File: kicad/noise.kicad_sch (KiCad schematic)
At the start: 9 parts, among them Q10 2N3904, Q9 2N3904

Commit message: component positioning mostly done
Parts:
- C51: footprint rumblesan-standard-parts:C_Rect_L7.0mm_W3.5mm_P5.00mm -> rumblesan-standard-parts:C_Rect_L7.0mm_W2.5mm_P5.00mm
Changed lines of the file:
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@@
     (property "Reference" "C51" (id 0) (at 93.98 72.8812 90))
     (property "Value" "100nF" (id 1) (at 93.98 75.4181 90))
-    (property "Footprint" "rumblesan-standard-parts:C_Rect_L7.0mm_W3.5mm_P5.00mm" (id 2) (at 92.71 73.025 90)
+    (property "Footprint" "rumblesan-standard-parts:C_Rect_L7.0mm_W2.5mm_P5.00mm" (id 2) (at 92.71 73.025 90)
       (effects (font (size 1.27 1.27)) hide)
     )

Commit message: initial layout done
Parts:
- C52: footprint rumblesan-standard-parts:C_Rect_L7.0mm_W3.5mm_P5.00mm -> rumblesan-standard-parts:C_Rect_L7.0mm_W2.5mm_P5.00mm
- Q10: value 2N3904 -> BC549C
- R120: value 1k -> 47r
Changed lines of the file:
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@@
       (effects (font (size 1.27 1.27)) (justify left))
     )
-    (property "Value" "2N3904" (id 1) (at 115.3414 80.4422 0)
+    (property "Value" "BC549C" (id 1) (at 115.3414 80.4422 0)
       (effects (font (size 1.27 1.27)) (justify left))
     )
@@
       (effects (font (size 1.27 1.27)) (justify left))
     )
-    (property "Value" "1k" (id 1) (at 114.808 91.8722 0)
+    (property "Value" "47r" (id 1) (at 114.808 91.8722 0)
       (effects (font (size 1.27 1.27)) (justify left))
     )
@@
     (property "Reference" "C52" (id 0) (at 123.19 66.5312 90))
     (property "Value" "47nF" (id 1) (at 123.19 69.0681 90))
-    (property "Footprint" "rumblesan-standard-parts:C_Rect_L7.0mm_W3.5mm_P5.00mm" (id 2) (at 121.92 66.675 90)
+    (property "Footprint" "rumblesan-standard-parts:C_Rect_L7.0mm_W2.5mm_P5.00mm" (id 2) (at 121.92 66.675 90)
       (effects (font (size 1.27 1.27)) hide)
     )

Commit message: Full rejig to use attiny for divider
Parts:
- removed Q9: 2N3904, rumblesan-standard-parts:TO-92_Inline_Wide, symbol Transistor_BJT:2N3904
- removed R116: 100k, rumblesan-standard-parts:R_Axial_DIN0207_L6.3mm_D2.5mm_P10.16mm_Horizontal, symbol rumblesan-standard-parts:R
- added Q9: BC547, rumblesan-standard-parts:TO-92_Inline_Wide, symbol Transistor_BJT:BC547
- added RV23: 200k, rumblesan-standard-parts:Potentiometer_THT_Bourns_3306P_Vertical, symbol rumblesan-standard-parts:R_Potentiometer_Trim
- C51: Spec ceramic C0G -> ceramic X7R
- C52: value 47nF -> 100nF; Spec ceramic C0G -> ceramic X7R
- R120: value 47r -> 22r
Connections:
- net GND: now also Q9.2 (B)
- net VCC: now also RV23.2
- net at C51.1: now also Q9.3 (E), RV23.1
- no-connect marks 1 -> 2
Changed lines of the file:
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@@
   )
   (no_connect (at 82.55 91.44))
+  (no_connect (at 82.55 64.77))
   (wire (pts (xy 113.03 60.96) (xy 113.03 63.5))
     (stroke (width 0) (type default) (color 0 0 0 0))
   )
-  (wire (pts (xy 82.55 76.2) (xy 82.55 78.74))
+  (wire (pts (xy 82.55 72.39) (xy 82.55 78.74))
     (stroke (width 0) (type default) (color 0 0 0 0))
   )
@@
     (stroke (width 0) (type default) (color 0 0 0 0))
   )
+  (wire (pts (xy 74.93 68.58) (xy 78.74 68.58))
+    (stroke (width 0) (type default) (color 0 0 0 0))
+  )
   (wire (pts (xy 127 72.39) (xy 132.08 72.39))
     (stroke (width 0) (type default) (color 0 0 0 0))
@@
     (stroke (width 0) (type default) (color 0 0 0 0))
   )
-  (wire (pts (xy 82.55 66.04) (xy 82.55 68.58))
-    (stroke (width 0) (type default) (color 0 0 0 0))
-  )
   (wire (pts (xy 113.03 72.39) (xy 113.03 73.66))
     (stroke (width 0) (type default) (color 0 0 0 0))
@@
   )
   (wire (pts (xy 71.12 86.36) (xy 71.12 92.71))
+    (stroke (width 0) (type default) (color 0 0 0 0))
+  )
+  (wire (pts (xy 74.93 59.69) (xy 74.93 68.58))
     (stroke (width 0) (type default) (color 0 0 0 0))
   )
@@
     )
     (pin "1")
+  )
+  (symbol (lib_id "rumblesan-standard-parts:R_Potentiometer_Trim") (at 82.55 68.58 180) (unit 1)
+    (in_bom yes) (on_board yes) (fields_autoplaced)
+    (property "Reference" "RV23" (id 0) (at 84.328 67.7453 0)
+      (effects (font (size 1.27 1.27)) (justify right))
+    )
+    (property "Value" "200k" (id 1) (at 84.328 70.2822 0)
+      (effects (font (size 1.27 1.27)) (justify right))
+    )
+    (property "Footprint" "rumblesan-standard-parts:Potentiometer_THT_Bourns_3306P_Vertical" (id 2) (at 82.55 68.58 0)
+      (effects (font (size 1.27 1.27)) hide)
+    )
+    (property "Datasheet" "~" (id 3) (at 82.55 68.58 0)
+      (effects (font (size 1.27 1.27)) hide)
+    )
+    (property "Name" "" (id 4) (at 78.74 78.74 0))
+    (property "Spec" "single turn" (id 5) (at 82.55 68.58 0)
+      (effects (font (size 1.27 1.27)) hide)
+    )
+    (pin "1")
+    (pin "2")
+    (pin "3")
   )
   (symbol (lib_id "rumblesan-standard-parts:R") (at 101.6 86.36 0) (unit 1)
@@
       (effects (font (size 1.27 1.27)) hide)
     )
-    (property "Spec" "ceramic C0G" (id 4) (at 93.98 74.93 90)
+    (property "Spec" "ceramic X7R" (id 4) (at 93.98 74.93 90)
       (effects (font (size 1.27 1.27)) hide)
     )
@@
     (pin "1")
   )
-  (symbol (lib_id "power:VCC") (at 82.55 66.04 0) (unit 1)
-    (in_bom yes) (on_board yes) (fields_autoplaced)
-    (property "Reference" "#PWR0162" (id 0) (at 82.55 69.85 0)
-      (effects (font (size 1.27 1.27)) hide)
-    )
-    (property "Value" "VCC" (id 1) (at 82.55 62.4642 0))
-    (property "Footprint" "" (id 2) (at 82.55 66.04 0)
-      (effects (font (size 1.27 1.27)) hide)
-    )
-    (property "Datasheet" "" (id 3) (at 82.55 66.04 0)
+  (symbol (lib_id "power:VCC") (at 74.93 59.69 0) (unit 1)
+    (in_bom yes) (on_board yes) (fields_autoplaced)
+    (property "Reference" "#PWR0162" (id 0) (at 74.93 63.5 0)
+      (effects (font (size 1.27 1.27)) hide)
+    )
+    (property "Value" "VCC" (id 1) (at 74.93 56.1142 0))
+    (property "Footprint" "" (id 2) (at 74.93 59.69 0)
+      (effects (font (size 1.27 1.27)) hide)
+    )
+    (property "Datasheet" "" (id 3) (at 74.93 59.69 0)
       (effects (font (size 1.27 1.27)) hide)
     )
@@
       (effects (font (size 1.27 1.27)) (justify left))
     )
-    (property "Value" "47r" (id 1) (at 114.808 91.8722 0)
+    (property "Value" "22r" (id 1) (at 114.808 91.8722 0)
       (effects (font (size 1.27 1.27)) (justify left))
     )
@@
     (pin "1")
   )
-  (symbol (lib_id "rumblesan-standard-parts:R") (at 82.55 72.39 0) (unit 1)
-    (in_bom yes) (on_board yes) (fields_autoplaced)
-    (property "Reference" "R116" (id 0) (at 84.328 71.5553 0)
-      (effects (font (size 1.27 1.27)) (justify left))
-    )
-    (property "Value" "100k" (id 1) (at 84.328 74.0922 0)
-      (effects (font (size 1.27 1.27)) (justify left))
-    )
-    (property "Footprint" "rumblesan-standard-parts:R_Axial_DIN0207_L6.3mm_D2.5mm_P10.16mm_Horizontal" (id 2) (at 85.09 74.93 90)
-      (effects (font (size 1.27 1.27)) hide)
-    )
-    (property "Datasheet" "~" (id 3) (at 88.9 72.39 90)
-      (effects (font (size 1.27 1.27)) hide)
-    )
-    (property "Tolerance" "1%" (id 4) (at 87.63 78.74 90)
-      (effects (font (size 1.27 1.27)) hide)
-    )
-    (property "Power" "0.5W" (id 5) (at 87.63 64.77 90)
-      (effects (font (size 1.27 1.27)) hide)
-    )
-    (property "Spec" "metal film" (id 6) (at 87.63 72.39 90)
-      (effects (font (size 1.27 1.27)) hide)
-    )
-    (pin "1")
-    (pin "2")
+  (symbol (lib_id "Transistor_BJT:BC547") (at 80.01 86.36 0) (mirror x) (unit 1)
+    (in_bom yes) (on_board yes) (fields_autoplaced)
+    (property "Reference" "Q9" (id 0) (at 84.8614 85.5253 0)
+      (effects (font (size 1.27 1.27)) (justify left))
+    )
+    (property "Value" "BC547" (id 1) (at 84.8614 88.0622 0)
+      (effects (font (size 1.27 1.27)) (justify left))
+    )
+    (property "Footprint" "rumblesan-standard-parts:TO-92_Inline_Wide" (id 2) (at 85.09 84.455 0)
+      (effects (font (size 1.27 1.27) italic) (justify left) hide)
+    )
+    (property "Datasheet" "https://www.onsemi.com/pub/Collateral/BC550-D.pdf" (id 3) (at 80.01 86.36 0)
+      (effects (font (size 1.27 1.27)) (justify left) hide)
+    )
+    (pin "1")
+    (pin "2")
+    (pin "3")
   )
   (symbol (lib_id "power:GND") (at 113.03 96.52 0) (mirror y) (unit 1)
@@
     (in_bom yes) (on_board yes) (fields_autoplaced)
     (property "Reference" "C52" (id 0) (at 123.19 66.5312 90))
-    (property "Value" "47nF" (id 1) (at 123.19 69.0681 90))
+    (property "Value" "100nF" (id 1) (at 123.19 69.0681 90))
     (property "Footprint" "rumblesan-standard-parts:C_Rect_L7.0mm_W2.5mm_P5.00mm" (id 2) (at 121.92 66.675 90)
       (effects (font (size 1.27 1.27)) hide)
@@
       (effects (font (size 1.27 1.27)) hide)
     )
-    (property "Spec" "ceramic C0G" (id 4) (at 123.19 68.58 90)
+    (property "Spec" "ceramic X7R" (id 4) (at 123.19 68.58 90)
       (effects (font (size 1.27 1.27)) hide)
     )
@@
     (pin "2")
   )
-  (symbol (lib_id "Transistor_BJT:2N3904") (at 80.01 86.36 0) (mirror x) (unit 1)
-    (in_bom yes) (on_board yes)
-    (property "Reference" "Q9" (id 0) (at 73.66 83.82 0)
-      (effects (font (size 1.27 1.27)) (justify left))
-    )
-    (property "Value" "2N3904" (id 1) (at 71.12 81.28 0)
-      (effects (font (size 1.27 1.27)) (justify left))
-    )
-    (property "Footprint" "rumblesan-standard-parts:TO-92_Inline_Wide" (id 2) (at 85.09 84.455 0)
-      (effects (font (size 1.27 1.27) italic) (justify left) hide)
-    )
-    (property "Datasheet" "https://www.onsemi.com/pub/Collateral/2N3903-D.PDF" (id 3) (at 80.01 86.36 0)
-      (effects (font (size 1.27 1.27)) (justify left) hide)
-    )
-    (pin "1")
-    (pin "2")
-    (pin "3")
-  )
   (symbol (lib_id "rumblesan-standard-parts:R") (at 113.03 67.31 0) (unit 1)

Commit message: Changing name to the mercurial machine
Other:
- title: (none) -> The Mercurial Machine
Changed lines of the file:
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@@
   (paper "A4")
   (title_block
+    (title "The Mercurial Machine")
+    (date "2023-05-13")
+    (rev "r02")
     (comment 2 "creativecommons.org/licenses/by/4.0/")
     (comment 3 "License: CC BY 4.0")

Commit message: geographically reannotate parts
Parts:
- renumbered C51 to C1, C52 to C2, Q9 to Q1, Q10 to Q2, R119 to R12, R117 to R3, R120 to R4, R118 to R6, RV23 to RV1
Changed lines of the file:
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@@
   (symbol (lib_id "rumblesan-standard-parts:R") (at 101.6 72.39 0) (unit 1)
     (in_bom yes) (on_board yes) (fields_autoplaced)
-    (property "Reference" "R117" (id 0) (at 103.378 71.5553 0)
+    (property "Reference" "R3" (id 0) (at 103.378 71.5553 0)
       (effects (font (size 1.27 1.27)) (justify left))
     )
@@
   (symbol (lib_id "rumblesan-standard-parts:R_Potentiometer_Trim") (at 82.55 68.58 180) (unit 1)
     (in_bom yes) (on_board yes) (fields_autoplaced)
-    (property "Reference" "RV23" (id 0) (at 84.328 67.7453 0)
+    (property "Reference" "RV1" (id 0) (at 84.328 67.7453 0)
       (effects (font (size 1.27 1.27)) (justify right))
     )
@@
   (symbol (lib_id "rumblesan-standard-parts:R") (at 101.6 86.36 0) (unit 1)
     (in_bom yes) (on_board yes) (fields_autoplaced)
-    (property "Reference" "R118" (id 0) (at 103.378 85.5253 0)
+    (property "Reference" "R6" (id 0) (at 103.378 85.5253 0)
       (effects (font (size 1.27 1.27)) (justify left))
     )
@@
   (symbol (lib_id "rumblesan-standard-parts:C") (at 93.98 78.74 90) (unit 1)
     (in_bom yes) (on_board yes) (fields_autoplaced)
-    (property "Reference" "C51" (id 0) (at 93.98 72.8812 90))
+    (property "Reference" "C1" (id 0) (at 93.98 72.8812 90))
     (property "Value" "100nF" (id 1) (at 93.98 75.4181 90))
     (property "Footprint" "rumblesan-standard-parts:C_Rect_L7.0mm_W2.5mm_P5.00mm" (id 2) (at 92.71 73.025 90)
@@
   (symbol (lib_id "Transistor_BJT:2N3904") (at 110.49 78.74 0) (unit 1)
     (in_bom yes) (on_board yes) (fields_autoplaced)
-    (property "Reference" "Q10" (id 0) (at 115.3414 77.9053 0)
+    (property "Reference" "Q2" (id 0) (at 115.3414 77.9053 0)
       (effects (font (size 1.27 1.27)) (justify left))
     )
@@
   (symbol (lib_id "rumblesan-standard-parts:R") (at 113.03 90.17 0) (unit 1)
     (in_bom yes) (on_board yes) (fields_autoplaced)
-    (property "Reference" "R120" (id 0) (at 114.808 89.3353 0)
+    (property "Reference" "R4" (id 0) (at 114.808 89.3353 0)
       (effects (font (size 1.27 1.27)) (justify left))
     )
@@
   (symbol (lib_id "Transistor_BJT:BC547") (at 80.01 86.36 0) (mirror x) (unit 1)
     (in_bom yes) (on_board yes) (fields_autoplaced)
-    (property "Reference" "Q9" (id 0) (at 84.8614 85.5253 0)
+    (property "Reference" "Q1" (id 0) (at 84.8614 85.5253 0)
       (effects (font (size 1.27 1.27)) (justify left))
     )
@@
   (symbol (lib_id "rumblesan-standard-parts:C") (at 123.19 72.39 90) (unit 1)
     (in_bom yes) (on_board yes) (fields_autoplaced)
-    (property "Reference" "C52" (id 0) (at 123.19 66.5312 90))
+    (property "Reference" "C2" (id 0) (at 123.19 66.5312 90))
     (property "Value" "100nF" (id 1) (at 123.19 69.0681 90))
     (property "Footprint" "rumblesan-standard-parts:C_Rect_L7.0mm_W2.5mm_P5.00mm" (id 2) (at 121.92 66.675 90)
@@
   (symbol (lib_id "rumblesan-standard-parts:R") (at 113.03 67.31 0) (unit 1)
     (in_bom yes) (on_board yes) (fields_autoplaced)
-    (property "Reference" "R119" (id 0) (at 114.808 66.4753 0)
-      (effects (font (size 1.27 1.27)) (justify left))
-    )
+    (property "Reference" "R12" (id 0) (at 114.808 66.4753 0)
+      (effects (font (size 1.27 1.27)) (justify left))
+    )

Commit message: Changing name again
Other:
- title: The Mercurial Machine -> Ouroboros
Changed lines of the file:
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@@
   (paper "A4")
   (title_block
-    (title "The Mercurial Machine")
+    (title "Ouroboros")
     (date "2023-05-13")
     (rev "r02")

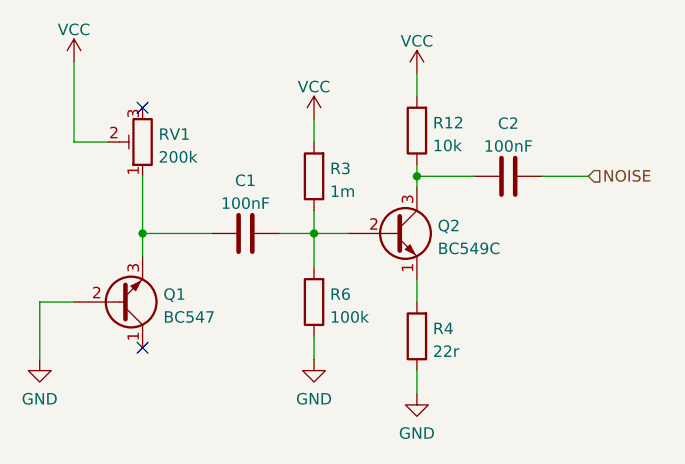
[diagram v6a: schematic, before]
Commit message: Updating for kicad 7
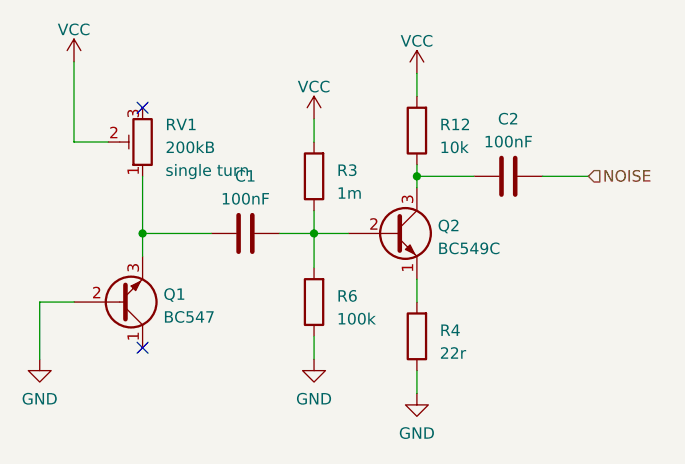
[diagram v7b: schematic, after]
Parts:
- C1, C2: footprint rumblesan-standard-parts:C_Rect_L7.0mm_W2.5mm_P5.00mm -> Rumblesan_Standard_Parts:C_Rect_L7.0mm_W2.5mm_P5.00mm; symbol rumblesan-standard-parts:C -> Rumblesan Standard Parts:C; Spec ceramic X7R -> ceramic C0G
- Q1, Q2: footprint rumblesan-standard-parts:TO-92_Inline_Wide -> Rumblesan_Standard_Parts:TO-92_Inline_Wide
- R12, R3, R4, R6: footprint rumblesan-standard-parts:R_Axial_DIN0207_L6.3mm_D2.5mm_P10.16mm_Horizontal -> Rumblesan_Standard_Parts:R_Axial_DIN0207_L6.3mm_D2.5mm_P10.16mm_Horizontal; symbol rumblesan-standard-parts:R -> Rumblesan Standard Parts:R
- RV1: value 200k -> 200kB; footprint rumblesan-standard-parts:Potentiometer_THT_Bourns_3306P_Vertical -> Rumblesan_Standard_Parts:Potentiometer_THT_Bourns_3306P_Vertical; symbol rumblesan-standard-parts:R_Potentiometer_Trim -> Rumblesan Standard Parts:R_Potentiometer_Trim

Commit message: Minor tweaks to rev2 values
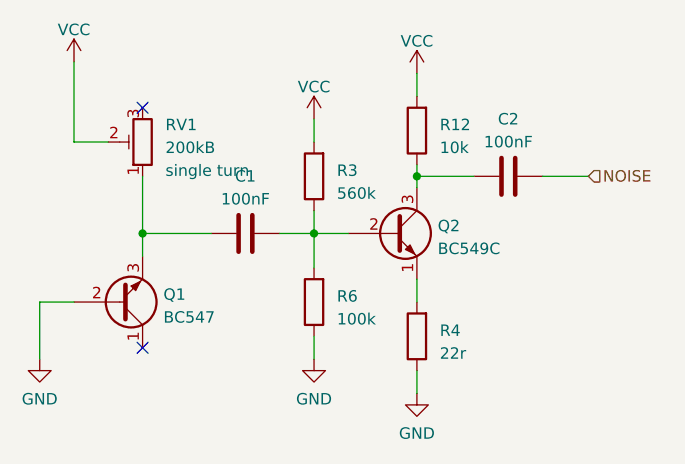
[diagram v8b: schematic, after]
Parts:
- R3: value 1m -> 560k
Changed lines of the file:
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@@
       (effects (font (size 1.27 1.27)) (justify left))
     )
-    (property "Value" "1m" (at 104.14 74.295 0)
+    (property "Value" "560k" (at 104.14 74.295 0)
       (effects (font (size 1.27 1.27)) (justify left))
     )
